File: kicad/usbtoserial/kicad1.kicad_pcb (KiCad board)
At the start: 2 copper layers, 41.9 x 20.3 mm, 7 parts, among them IC1 FT232RL, J1 USB_A, J2 Conn_01x06_Male

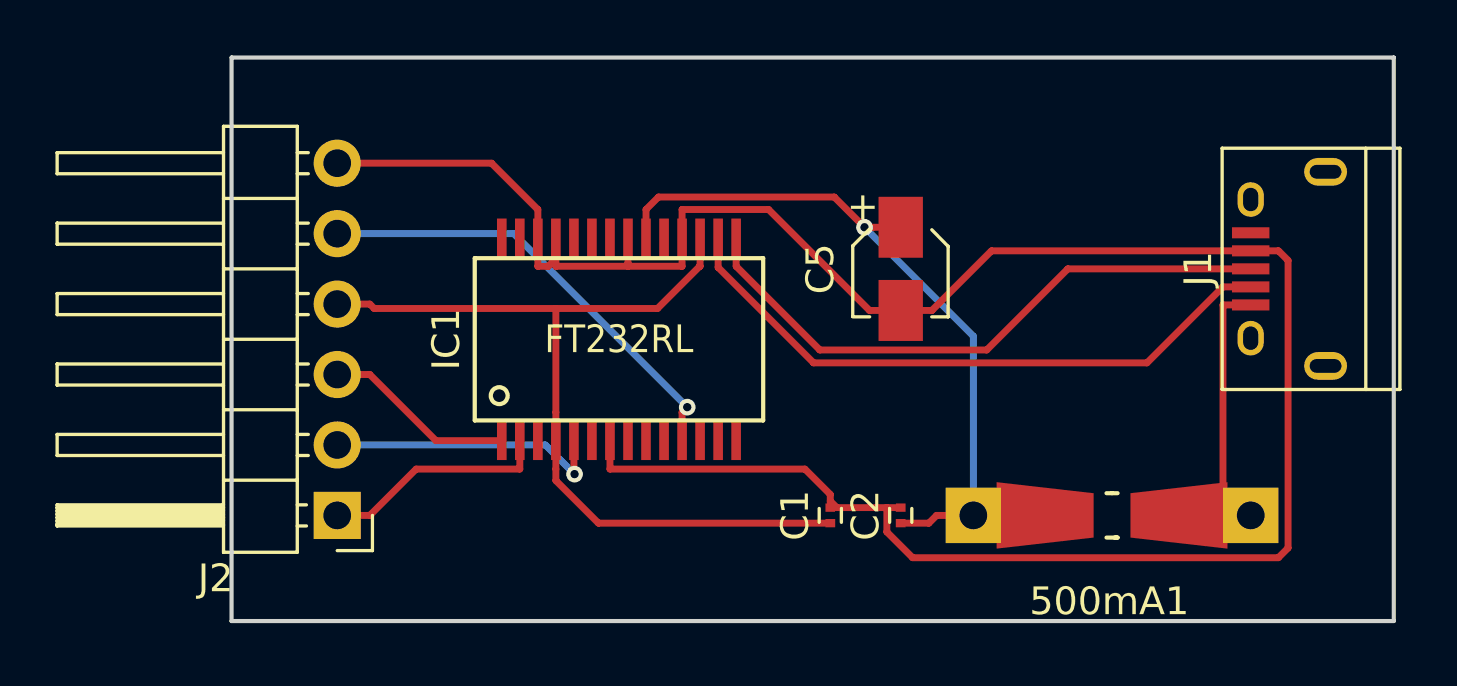
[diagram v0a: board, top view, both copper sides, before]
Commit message: routing in 1 layer
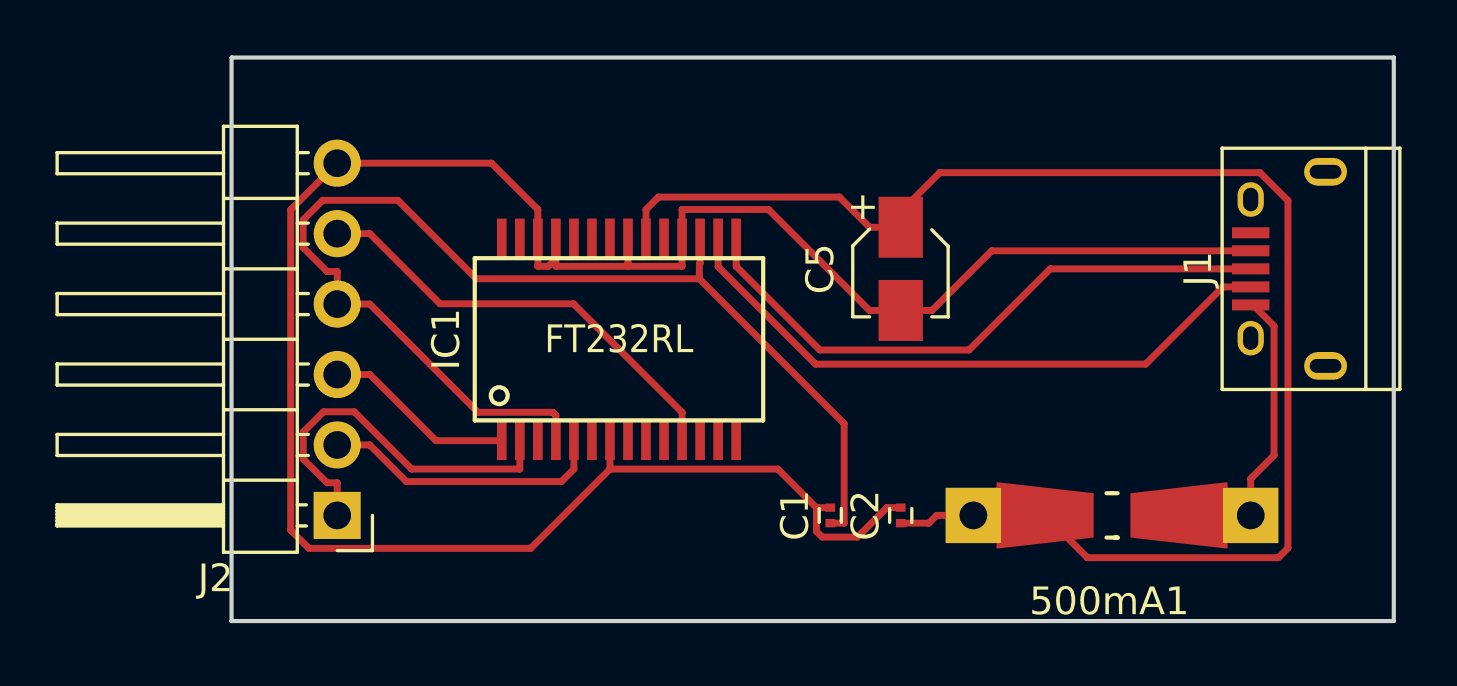
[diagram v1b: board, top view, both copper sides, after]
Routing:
- net Net-(500mA1-Pad2): track 28.2 -> 54.0 mm, vias 1 -> 0
- net Net-(C1-Pad1): track 31.5 -> 42.9 mm
- net Net-(IC1-Pad2): track 8.30 -> 13.7 mm
- net Earth: track 82.5 -> 83.1 mm
- net Net-(IC1-Pad11): track 16.5 -> 16.1 mm, vias 1 -> 0
- net Net-(IC1-Pad5): track 10.2 -> 10.3 mm, vias 1 -> 0
